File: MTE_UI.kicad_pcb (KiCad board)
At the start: 2 copper layers, 130 x 75 mm, 202 parts, among them J101 Conn_02x10_Odd_Even, J102 Conn_02x03_Odd_Even, J103 Conn_01x10, J401 Conn_01x03, J402 Conn_01x04, Q201 BSS138, Q202 BSS84, Q401 BSS138, Q402 BSS138, Q403 BSS138, Q404 BSS138, Q405 BSS138, Q406 BSS84, Q407 BSS84, Q408 BSS138, SW201 B3W-9000-RG2N, SW202 B3W-9000-RG2N, SW203 B3W-9000-RG2N, SW204 B3W-9000-RG2N, SW205 Rotary_Encoder_Switch, SW206 Rotary_Encoder_Switch, U201 74LVC1G125, U202 TLV271, U301 74LVC1G126, U302 74LVC1G125, U303 74LVC273, U304 74LVC2G14, U305 NCP1117-ADJ_TO252, U306 SN65MLVD203, U307 SN65LVDS1, U308 PCA9509DP, U309 24LC16, U310 24LC16, U311 SN65MLVD200A, U401 STM32F101VCTx, U402 LM4132-2, U403 74LVC1G57, U404 74LVC1G57, U405 74LVC1G57, U406 74LVC2G14, Y401 8MHz, Y402 32.768kHz

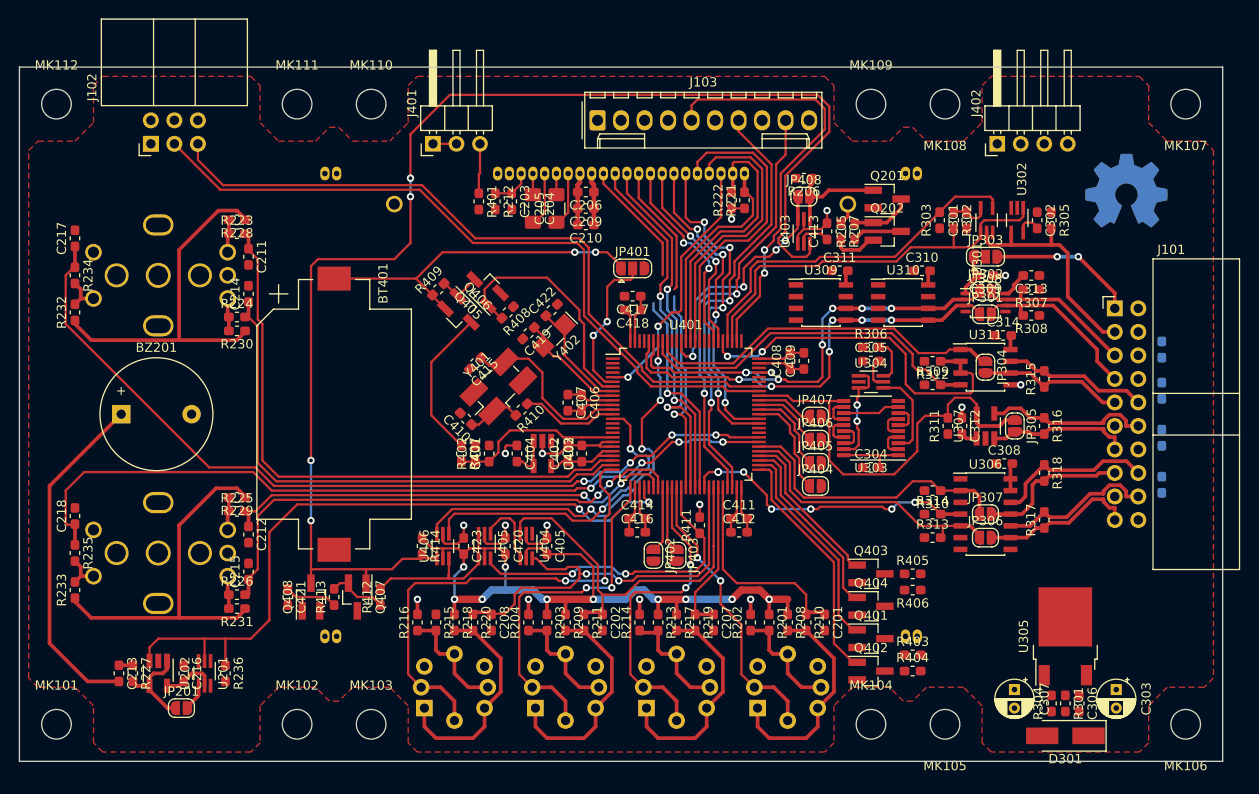
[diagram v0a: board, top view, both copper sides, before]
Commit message: Revised schematic, initial PCB layout complete
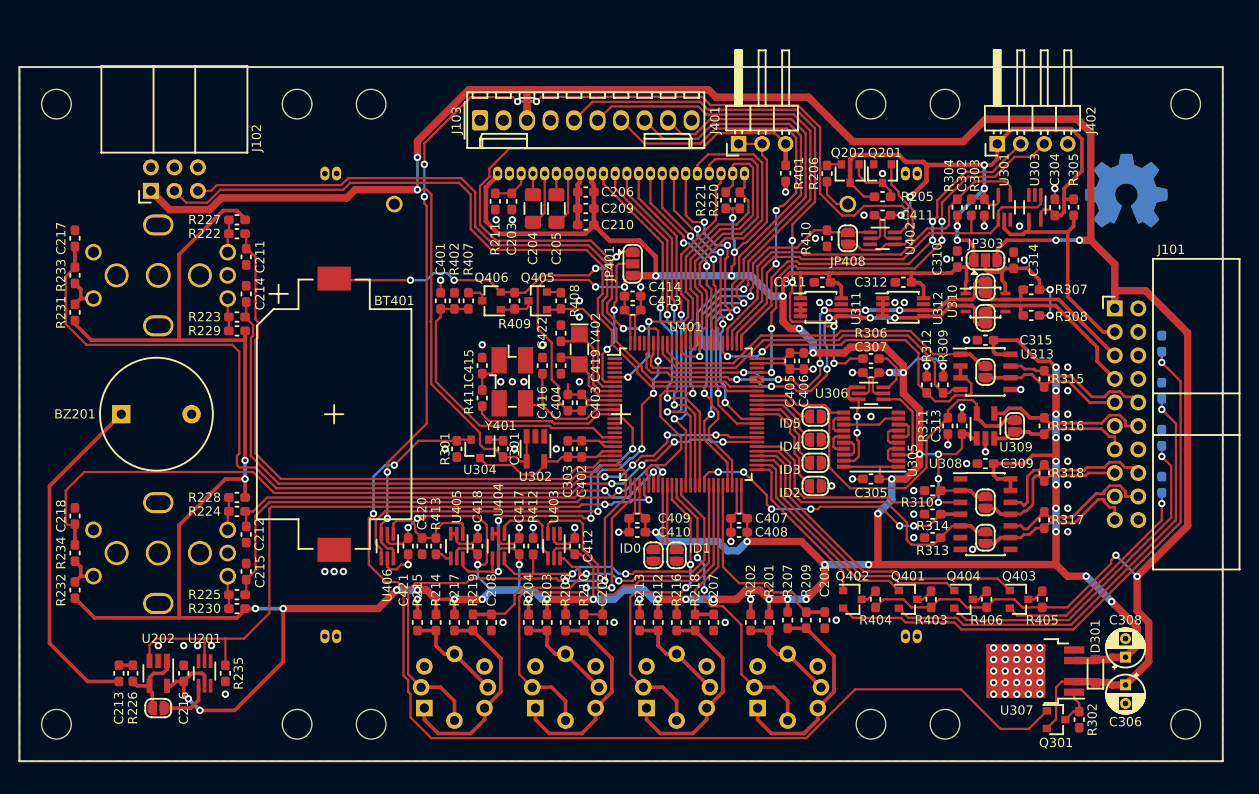
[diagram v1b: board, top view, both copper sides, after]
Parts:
- removed the C305 at (207.0, 74.2)
- removed the C404 at (168.8, 84.2)
- removed the C406 at (175.8, 78.8)
- removed the C413 at (202.2, 60.2)
- removed C423: 100n, Capacitor_SMD:C_0603_1608Metric_Pad1.05x0.95mm_HandSolder
- removed Q407: BSS84, Package_TO_SOT_SMD:SOT-23_Handsoldering
- removed Q408: BSS138, Package_TO_SOT_SMD:SOT-23_Handsoldering
- removed R236, R414: 100k, Resistor_SMD:R_0603_1608Metric_Pad1.05x0.95mm_HandSolder
- removed the U305 at (228.0, 104.0)
- removed the U308 at (219.4, 67.9)
- removed the U309 at (201.6, 67.9)
- removed the U403 at (199.8, 60.2)
- added C304: 100n, Capacitor_SMD:C_0603_1608Metric_Pad1.05x0.95mm_HandSolder, F.Cu at (226.9, 57.6)
- added C308: 10u, Capacitor_THT:CP_Radial_D4.0mm_P2.00mm, F.Cu at (234.5, 106.2)
- added C411: 100n, Capacitor_SMD:C_0603_1608Metric_Pad1.05x0.95mm_HandSolder, F.Cu at (208.2, 58.5)
- added C417: 100n, Capacitor_SMD:C_0603_1608Metric_Pad1.05x0.95mm_HandSolder, F.Cu at (169.0, 94.2)
- added C418: 100n, Capacitor_SMD:C_0603_1608Metric_Pad1.05x0.95mm_HandSolder, F.Cu at (164.5, 94.2)
- added Q301: BSS84, Package_TO_SOT_SMD:SOT-23, F.Cu at (227.0, 113.0)
- added U303: 74LVC1G125, Package_TO_SOT_SMD:SOT-353_SC-70-5_Handsoldering, F.Cu at (224.7, 57.6)
- added U304: STM809T, Package_TO_SOT_SMD:SOT-23, F.Cu at (164.8, 83.8)
- added U307: NCP5661DT33, Package_TO_SOT_SMD:TO-252-4, F.Cu at (224.8, 107.8)
- added U312: 24LC16, Package_SO:MSOP-8_3x3mm_P0.65mm, F.Cu at (210.5, 68.4)
- added U313: SN65MLVD200A, Package_SO:SOIC-8_3.9x4.9mm_P1.27mm, F.Cu at (219.4, 75.4)
- added U404: 74LVC1G57, Package_TO_SOT_SMD:SOT-363_SC-70-6_Handsoldering, F.Cu at (166.8, 94.2)
- C301, C420: value 100n -> 4u7
- C303: value 10u -> 1u; footprint Capacitor_THT:CP_Radial_D4.0mm_P2.00mm -> Capacitor_SMD:C_0603_1608Metric_Pad1.05x0.95mm_HandSolder
- C306: value 1u -> 10u; footprint Capacitor_SMD:C_0603_1608Metric_Pad1.05x0.95mm_HandSolder -> Capacitor_THT:CP_Radial_D4.0mm_P2.00mm
- C307: value 10u -> 100n; footprint Capacitor_THT:CP_Radial_D4.0mm_P2.00mm -> Capacitor_SMD:C_0603_1608Metric_Pad1.05x0.95mm_HandSolder
- C403: value 1u -> 100n
- C410: renamed from C405; value 100n -> 4u7
- C413: renamed from C418; value 4u7 -> 100n
- C414: renamed from C410; value 12p -> 4u7
- C415: value 22p -> 12p
- C416: value 4u7 -> 22p
- C421: value 4u7 -> 100n
- D301: value S1A -> BAS316; footprint Diode_SMD:D_SMA_Handsoldering -> Diode_SMD:D_SOD-323_HandSoldering
- Q201, Q202, Q401, Q402, Q403, Q404, Q405, Q406: footprint Package_TO_SOT_SMD:SOT-23_Handsoldering -> Package_TO_SOT_SMD:SOT-23
- R206: value 100k -> 10R
- R207: value 10R -> 33k
- R209, R218, R233: value 33k -> 3k3
- R211: value 3k3 -> 1M
- R212: value 1M -> 1k5
- R216: value 1k5 -> 33k
- R220, R235: value 3k3 -> 100k
- R222: value 100k -> 3k3
- R226: value 3k3 -> 100R
- R227: value 100R -> 33k
- R301: value 300R -> R
- R302: value 100k -> R
- R304, R410: value 180R -> 100k
- R411: value 100k -> 180R
- R412: value 33k -> 100k
- U302: value 74LVC1G125 -> LM4132-2; footprint Package_TO_SOT_SMD:SOT-353_SC-70-5_Handsoldering -> Package_TO_SOT_SMD:SOT-23-5_HandSoldering
- U310: value 24LC16 -> PCA9509DP; footprint Package_SO:SOIC-8_3.9x4.9mm_P1.27mm -> Package_SO:TSSOP-8_3x3mm_P0.65mm
- U311: value SN65MLVD200A -> 24LC16; footprint Housings_SOIC:SOIC-8_3.9x4.9mm_Pitch1.27mm -> Package_SO:MSOP-8_3x3mm_P0.65mm
- U401: value STM32F101VCTx -> STM32F101VDTx
- U402: value LM4132-2 -> 74LVC1G57; footprint Package_TO_SOT_SMD:SOT-23-5_HandSoldering -> Package_TO_SOT_SMD:SOT-363_SC-70-6_Handsoldering
- moved R301 71.3 mm to (162.2, 83.8)
- moved C303 64.7 mm to (174.2, 83.8), turned to 90 degrees
- moved U302 57.6 mm to (170.8, 83.8)
- moved C301 55.8 mm to (167.2, 83.8), turned to 270 degrees
- moved R302 55.6 mm to (229.5, 113.0)
- moved R304 54.6 mm to (216.3, 57.6)
- moved R220 54.0 mm to (192.8, 56.9), turned to 90 degrees
- moved R222 53.6 mm to (138.5, 60.5), turned to 0 degrees
- moved R227 50.3 mm to (138.5, 59.0), turned to 180 degrees
- moved R212 48.8 mm to (184.0, 102.5)
- moved R211 46.5 mm to (166.4, 57.0)
- moved U402 43.5 mm to (208.2, 61.0), turned to 0 degrees
- moved R207 42.4 mm to (198.0, 102.2)
- moved R410 37.8 mm to (202.2, 61.0), turned to 270 degrees
- moved C307 37.6 mm to (207.0, 75.5), turned to 0 degrees
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- renumbered C304 to C305, C308 to C309, C309 to C310, C310 to C311, C311 to C312, C312 to C313, C313 to C314, C314 to C315, C407 to C404, C408 to C405, C409 to C406, C411 to C407, C412 to C408, C414 to C409, C417 to C412, U303 to U305, U304 to U306, U306 to U308, U307 to U309, U404 to U403
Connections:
- net /Microcontroller/SW_VBAT renamed /Microcontroller/EN_VBAT
- C301 pad 2: +3V3D -> +5V0D
- C303 pad 1: +5V0D -> +3V3A
- C306 pad 1: Net-(C306-Pad1) -> +5V0D
- C307 pad 1: +3V3D -> DGND
- C307 pad 2: DGND -> +3V3D
- C314 pad 2: Net-(C313-Pad2) -> Net-(C314-Pad2)
- C402 pad 1: Net-(C402-Pad1) -> +3V3A
- C403 pad 1: Net-(C402-Pad1) -> DGND
- C403 pad 2: DGND -> +3V3D
- C414 pad 1: Net-(C410-Pad1) -> DGND
- C414 pad 2: DGND -> +3V3D
- C415 pad 1: /Microcontroller/OSC_IN -> Net-(C415-Pad1)
- C416 pad 1: DGND -> /Microcontroller/OSC_IN
- C416 pad 2: +3V3D -> DGND
- C420 pad 2: +3V3D -> Net-(C420-Pad2)
- C421 pad 1: Net-(C421-Pad1) -> DGND
- C421 pad 2: DGND -> +3V3D
- J102 pad 1: +3V3D -> +5V0D
- J103 pad 1: /SYNC -> (no net)
- J103 pad 5: /FAN_PWM -> /SYNC
- J103 pad 6: DGND -> /PG
- J103 pad 7: /FAN1_RPM -> /FAN_PWM
- J103 pad 8: DGND -> /FAN0_RPM
- J103 pad 9: /FAN0_RPM -> /FAN1_RPM
- JP303 pad 2: Net-(C313-Pad2) -> Net-(C314-Pad2)
- R206 pad 1: /Microcontroller/LCD_BL -> Net-(DS201-Pad31)
- R206 pad 2: DGND -> Net-(Q202-Pad2)
- R207 pad 1: Net-(DS201-Pad31) -> +3V3D
- R207 pad 2: Net-(Q202-Pad2) -> Net-(R207-Pad2)
- R209 pad 1: +3V3D -> /Microcontroller/SW4
- R209 pad 2: Net-(R209-Pad2) -> Net-(R207-Pad2)
- R210 pad 1: /Microcontroller/SW4 -> /Microcontroller/SW2
- R211 pad 1: /Microcontroller/SW2 -> Net-(C203-Pad1)
- R211 pad 2: Net-(R209-Pad2) -> DGND
- R212 pad 1: Net-(C203-Pad1) -> +3V3D
- R212 pad 2: DGND -> Net-(R212-Pad2)
- R213 pad 1: +3V3D -> Net-(R212-Pad2)
- R213 pad 2: Net-(R213-Pad2) -> DGND
- R214 pad 1: Net-(R213-Pad2) -> +3V3D
- R214 pad 2: DGND -> Net-(R214-Pad2)
- R215 pad 1: +3V3D -> Net-(R214-Pad2)
- R215 pad 2: Net-(R215-Pad2) -> DGND
- R216 pad 1: Net-(R215-Pad2) -> +3V3D
- R216 pad 2: DGND -> Net-(R216-Pad2)
- R218 pad 1: +3V3D -> /Microcontroller/SW3
- R218 pad 2: Net-(R218-Pad2) -> Net-(R216-Pad2)
- R219 pad 1: /Microcontroller/SW3 -> /Microcontroller/SW1
- R220 pad 1: /Microcontroller/SW1 -> +3V3D
- R220 pad 2: Net-(R218-Pad2) -> /Microcontroller/LCD_~CS~
- R221 pad 2: /Microcontroller/LCD_~CS~ -> /Microcontroller/LCD_~RST~
- R222 pad 1: +3V3D -> Net-(R222-Pad1)
- R222 pad 2: /Microcontroller/LCD_~RST~ -> /Microcontroller/ENC1_A
- R223 pad 2: /Microcontroller/ENC1_A -> /Microcontroller/ENC1_B
- R224 pad 2: /Microcontroller/ENC1_B -> /Microcontroller/ENC2_A
- R225 pad 2: /Microcontroller/ENC2_A -> /Microcontroller/ENC2_B
- R226 pad 1: Net-(R226-Pad1) -> Net-(C213-Pad1)
- R226 pad 2: /Microcontroller/ENC2_B -> Net-(JP201-Pad1)
- R227 pad 1: Net-(C213-Pad1) -> +3V3D
- R227 pad 2: Net-(JP201-Pad1) -> Net-(R222-Pad1)
- R228 pad 2: Net-(R223-Pad1) -> Net-(R224-Pad1)
- R229 pad 2: Net-(R225-Pad1) -> Net-(R223-Pad1)
- R230 pad 2: Net-(R224-Pad1) -> Net-(R225-Pad1)
- R231 pad 2: Net-(R226-Pad1) -> Net-(R231-Pad2)
- R233 pad 1: +3V3D -> /Microcontroller/ENC1_S
- R233 pad 2: Net-(R233-Pad2) -> Net-(R231-Pad2)
- R234 pad 1: /Microcontroller/ENC1_S -> /Microcontroller/ENC2_S
- R235 pad 1: /Microcontroller/ENC2_S -> /Microcontroller/BZ
- R235 pad 2: Net-(R233-Pad2) -> DGND
- R301 pad 1: Net-(C306-Pad1) -> Net-(Q301-Pad1)
- R302 pad 1: +3V3D -> Net-(Q301-Pad3)
- R302 pad 2: /Microcontroller/1W-TX -> DGND
- R303 pad 2: /Microcontroller/1W-RX -> /Microcontroller/1W-TX
- R304 pad 2: Net-(C306-Pad1) -> /Microcontroller/1W-RX
- R307 pad 1: Net-(C313-Pad2) -> Net-(C314-Pad2)
- R308 pad 1: Net-(C313-Pad2) -> Net-(C314-Pad2)
- R410 pad 1: /Microcontroller/OSC_OUT -> Net-(JP408-Pad1)
- R410 pad 2: Net-(C410-Pad1) -> DGND
- R411 pad 1: /Microcontroller/~BOOT_EN~ -> /Microcontroller/OSC_OUT
- R411 pad 2: DGND -> Net-(C415-Pad1)
- R412 pad 1: Net-(Q407-Pad2) -> /Microcontroller/~EN_BOOT~
- R412 pad 2: Net-(R412-Pad2) -> DGND
- R413 pad 1: Net-(C421-Pad1) -> Net-(C420-Pad2)
- R413 pad 2: Net-(Q407-Pad2) -> Net-(R413-Pad2)
- SW201 pad 1: Net-(R208-Pad2) -> Net-(R207-Pad2)
- SW201 pad 2: Net-(R208-Pad2) -> Net-(R207-Pad2)
- SW202 pad 1: Net-(R209-Pad2) -> Net-(R208-Pad2)
- SW202 pad 2: Net-(R209-Pad2) -> Net-(R208-Pad2)
- SW203 pad 1: Net-(R217-Pad2) -> Net-(R216-Pad2)
- SW203 pad 2: Net-(R217-Pad2) -> Net-(R216-Pad2)
- SW203 pad 5: Net-(R213-Pad2) -> Net-(R212-Pad2)
- SW203 pad 8: Net-(R213-Pad2) -> Net-(R212-Pad2)
- SW204 pad 1: Net-(R218-Pad2) -> Net-(R217-Pad2)
- SW204 pad 2: Net-(R218-Pad2) -> Net-(R217-Pad2)
- SW204 pad 5: Net-(R215-Pad2) -> Net-(R214-Pad2)
- SW204 pad 8: Net-(R215-Pad2) -> Net-(R214-Pad2)
- SW205 pad A: Net-(R223-Pad1) -> Net-(R222-Pad1)
- SW205 pad B: Net-(R224-Pad1) -> Net-(R223-Pad1)
- SW205 pad S1: Net-(R232-Pad2) -> Net-(R231-Pad2)
- SW206 pad A: Net-(R225-Pad1) -> Net-(R224-Pad1)
- SW206 pad B: Net-(R226-Pad1) -> Net-(R225-Pad1)
- SW206 pad S1: Net-(R233-Pad2) -> Net-(R232-Pad2)
- U302 pad 1: /Microcontroller/1W-TX -> (no net)
- U302 pad 3: DGND -> +5V0D
- U302 pad 4: /BUS_1-WIRE -> +5V0D
- U302 pad 5: +3V3D -> +3V3A
- U310 pad 1: DGND -> +3V3D
- U310 pad 2: DGND -> /Microcontroller/SCL
- U310 pad 3: DGND -> /Microcontroller/SDA
- U310 pad 5: /Microcontroller/SDA -> (no net)
- U310 pad 6: /Microcontroller/SCL -> /BUS_SDA
- U310 pad 7: DGND -> /BUS_SCL
- U310 pad 8: +3V3D -> Net-(C314-Pad2)
- U311 pad 1: /Microcontroller/TRIG_IN -> +3V3D
- U311 pad 2: /Microcontroller/TRIG_DIR -> DGND
- U311 pad 3: /Microcontroller/TRIG_DIR -> DGND
- U311 pad 4: /Microcontroller/TRIG_OUT -> DGND
- U311 pad 5: DGND -> /Microcontroller/SDA
- U311 pad 6: /BUS_TRIG_P -> /Microcontroller/SCL
- U311 pad 7: /BUS_TRIG_N -> DGND
- U401 pad 21: Net-(C402-Pad1) -> +3V3A
- U401 pad 22: Net-(C402-Pad1) -> +3V3A
- U401 pad 30: (no net) -> /PG
- U401 pad 37: /Microcontroller/~BOOT_EN~ -> /Microcontroller/~EN_BOOT~
- U402 pad 1: (no net) -> Net-(JP408-Pad1)
- U402 pad 3: +5V0D -> DGND
- U402 pad 4: +5V0D -> /Microcontroller/LCD_BL
- U402 pad 5: Net-(C402-Pad1) -> +3V3D
- U403 pad 4: Net-(U404-Pad4) -> Net-(U403-Pad4)
- U405 pad 1: Net-(U404-Pad4) -> Net-(C420-Pad2)
- U405 pad 3: +3V3D -> DGND
- U405 pad 4: Net-(R412-Pad2) -> Net-(R413-Pad2)
- U405 pad 6: /Microcontroller/~BOOT_EN~ -> /Microcontroller/NRST
- U406 pad 1: Net-(Q407-Pad1) -> Net-(C420-Pad2)
- U406 pad 3: Net-(R412-Pad2) -> Net-(U402-Pad6)
- U406 pad 4: /Microcontroller/NRST -> /Microcontroller/BOOT0
- U406 pad 6: /Microcontroller/BOOT0 -> Net-(U402-Pad6)
- Y401 pad 1: Net-(C410-Pad1) -> Net-(C415-Pad1)
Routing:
- net +3V3D: track 249.3 -> 689.1 mm, vias 12 -> 60
- net +5V0D: track 20.6 -> 287.5 mm, vias 2 -> 6
- net Net-(Q407-Pad1): track 143.3 -> 0.00 mm, vias 4 -> 0
- net Net-(U402-Pad6): track 0.00 -> 115.9 mm, vias 0 -> 6
- net Net-(Q301-Pad1): track 0.00 -> 115.5 mm, vias 0 -> 2
- net /PG: track 0.00 -> 76.9 mm, vias 0 -> 2
- net /Microcontroller/BOOT0: track 49.9 -> 123.1 mm, vias 4 -> 6
- net /SYNC: track 0.00 -> 62.2 mm, vias 0 -> 4
- net Net-(D402-Pad2): track 0.00 -> 61.5 mm, vias 0 -> 1
- net Net-(D401-Pad2): track 0.00 -> 49.1 mm, vias 0 -> 1
- net /Microcontroller/SWDIO: track 1.35 -> 49.3 mm, vias 1 -> 4
- net /Microcontroller/SWCLK: track 0.00 -> 43.8 mm, vias 0 -> 2
- net Net-(D404-Pad2): track 0.00 -> 36.7 mm, vias 0 -> 1
- net /Microcontroller/~EN_BOOT~: track 0.00 -> 34.9 mm, vias 0 -> 2
- net /Microcontroller/~BOOT_EN~: track 34.4 -> 0.00 mm, vias 2 -> 0
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- added copper zone on B.Cu, net DGND
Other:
- rule via_min_size: 0.4 -> 0.6
- board text added: "ID0"
- board text added: "ID1"
- board text added: "ID2"
- board text added: "ID3"
- board text added: "ID4"
- board text added: "ID5"
